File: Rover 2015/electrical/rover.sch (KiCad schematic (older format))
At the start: 16 parts, among them Q1 TIP120, Q2 TIP120, U1 HC-SR04, U2 ADXL345, U3 HMC5883L, U4 QTR-1A, U5 QTR-1A, U6 ARDUINO_MEGA

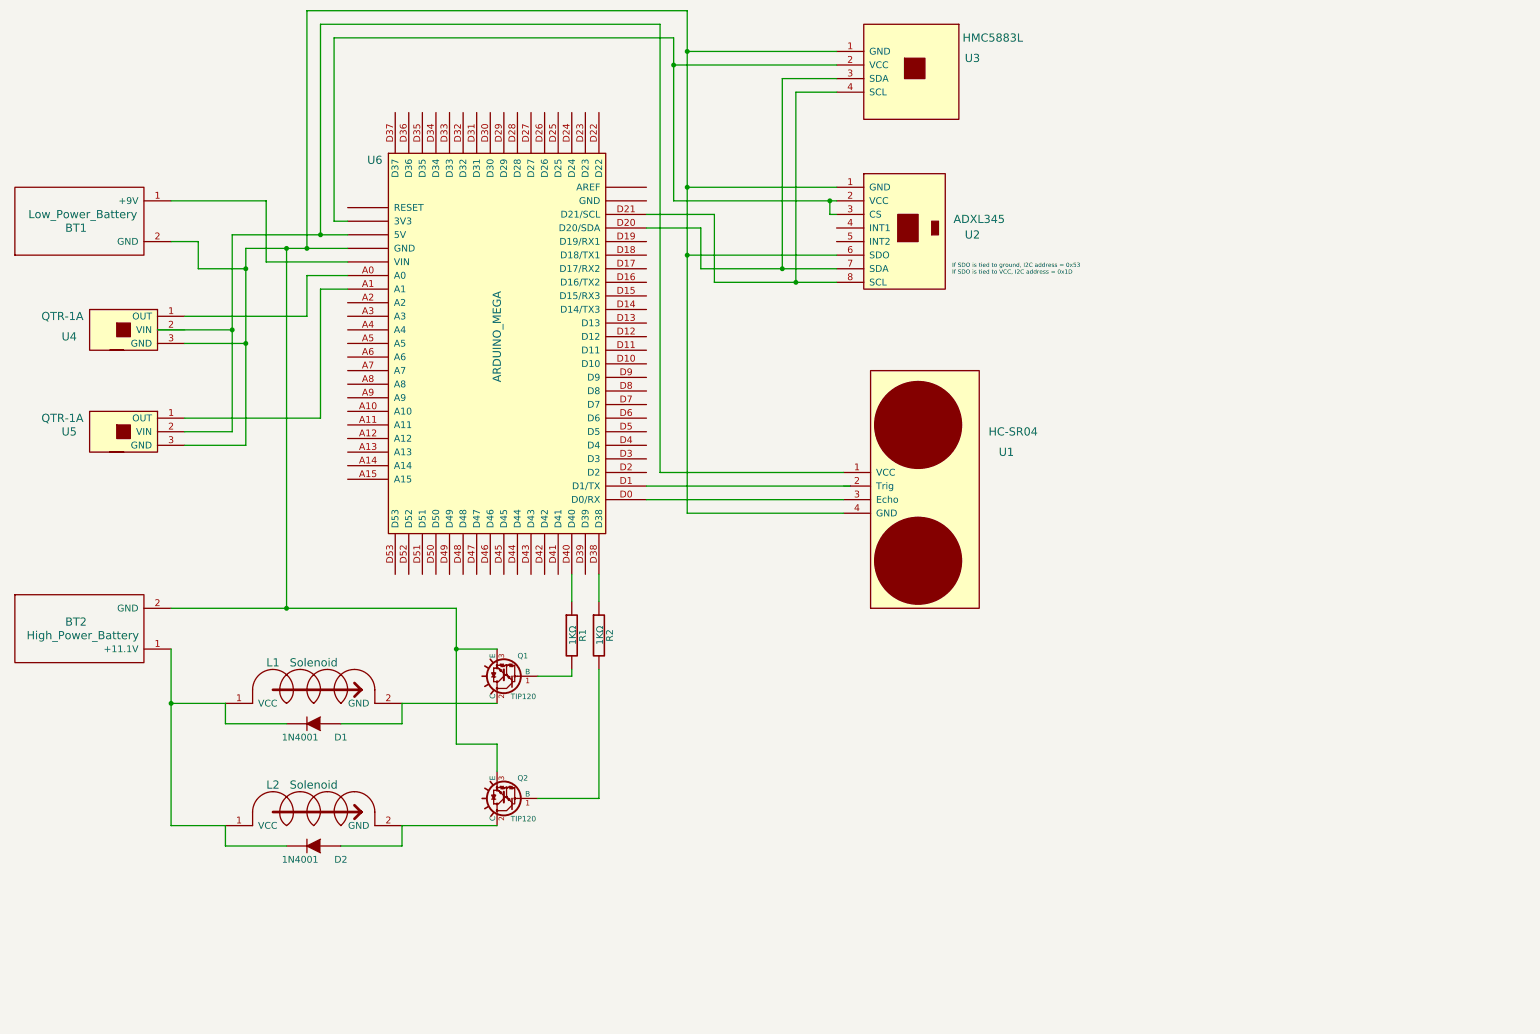
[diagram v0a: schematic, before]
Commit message: Motor and motor controller added, and block diagrams and flowcharts created
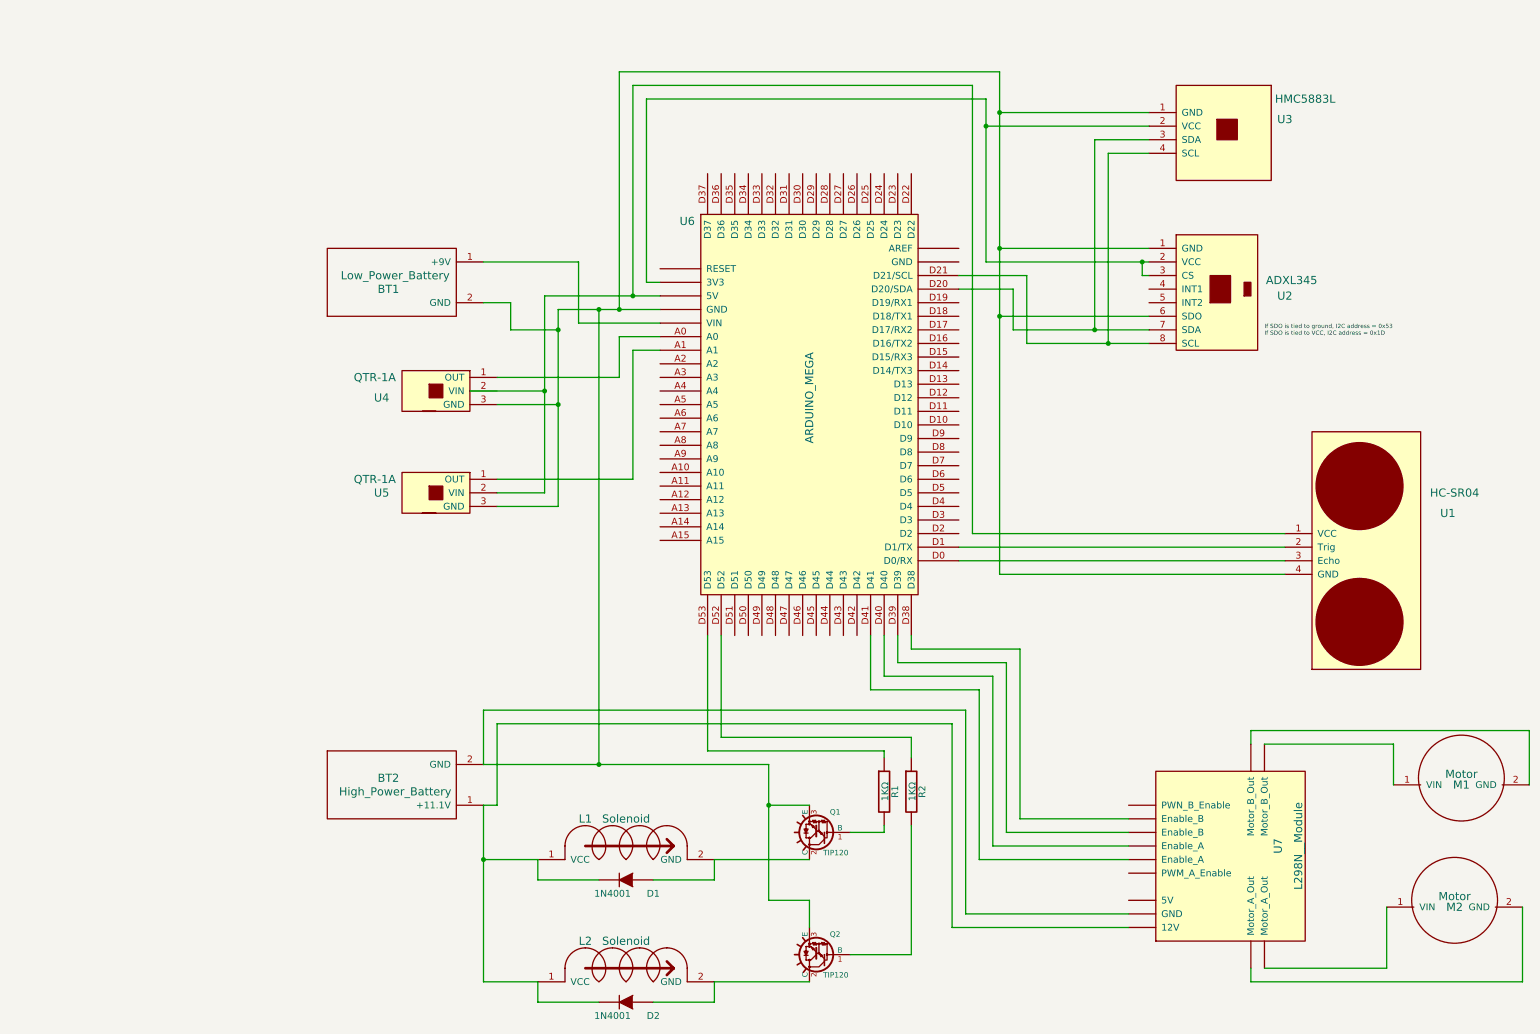
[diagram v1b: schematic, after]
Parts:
- added M1, M2: Motor, symbol Motor
- added U7: L298N__Module, symbol L298N__Module
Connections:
- net at U6.D1 (D1/TX): now also U1.2 (Trig)
- net at U6.D38: now also U7.~ (PWN_B_Enable); no longer R2.1
- net at U6.D39: now also U7.~ (PWN_B_Enable)
- net at U6.D40: now also U7.~ (PWN_B_Enable); no longer R1.1
- net at U6.D41: now also U7.~ (PWN_B_Enable)
- net at U6.D52: now also R2.1
- net at U6.D53: now also R1.1
- net at U6.~ (VIN): now also BT1.1 (+9V)
- net at BT1.2 (GND), BT2.2 (GND), Q1.3 (E)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: now also U7.~ (PWN_B_Enable)
- net at BT2.1 (+11.1V), D1.2 (K), D2.2 (K)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: now also U7.~ (PWN_B_Enable)
- new net: M1.1 (VIN), U7.~ (PWN_B_Enable)
- new net: M1.2 (GND), U7.~ (PWN_B_Enable)
- new net: M2.1 (VIN), U7.~ (PWN_B_Enable)
- new net: M2.2 (GND), U7.~ (PWN_B_Enable)
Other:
- moved on the sheet: BT1, BT2, D1, D2, L1, L2, Q1, Q2, R1, R2, U1, U2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
